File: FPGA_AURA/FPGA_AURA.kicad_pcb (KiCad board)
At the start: 10 copper layers, 50 x 50 mm, 191 parts, among them J1 ST5-40-1.00-L-D-P-TR, J100 USB_C_Receptacle_USB2.0_16P, J101 XT30PW-M, U1 XC7A35T-2FTG256C, U2 W25Q256JVEIQ, U200 ADP5014, U3 FT2232HQ, U4 TPS51200DRCR, U5 USBLC6-2SC6, U500 MT41K128M16JT-125_IT_K, U6 93LC56BT-I_SN, Y1 12MHz

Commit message: Continued DDR3 routing on top
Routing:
- net DDR3_A8: track 58.5 -> 76.5 mm
- net DDR3_BA1: track 0.57 -> 16.1 mm
- net DDR3_A3: track 3.18 -> 17.1 mm
- net DDR3_A0: track 4.63 -> 17.9 mm
- net DDR3_BA2: track 0.57 -> 8.20 mm
- net DDR3_A10: track 0.57 -> 5.79 mm
- net DDR3_CAS: track 0.57 -> 4.15 mm
- net DDR3_DQ1: track 49.4 -> 46.8 mm
- net DDR3_A12: track 0.57 -> 2.93 mm
- net DDR3_DQS0-: track 47.4 -> 46.5 mm
- net DDR3_ODT: track 1.27 -> 0.57 mm
- net DDR3_DQ2: track 47.3 -> 46.7 mm

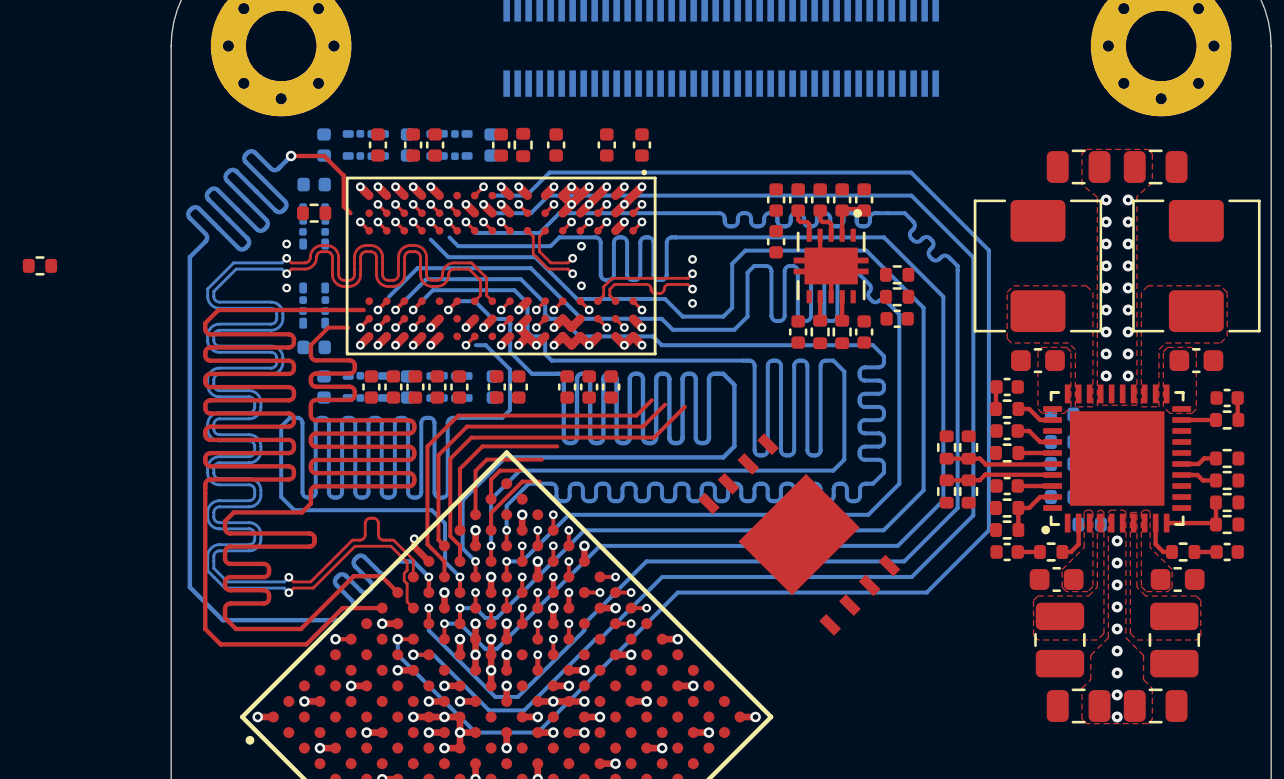
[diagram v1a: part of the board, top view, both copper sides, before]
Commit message: Continued DDR3 routing.
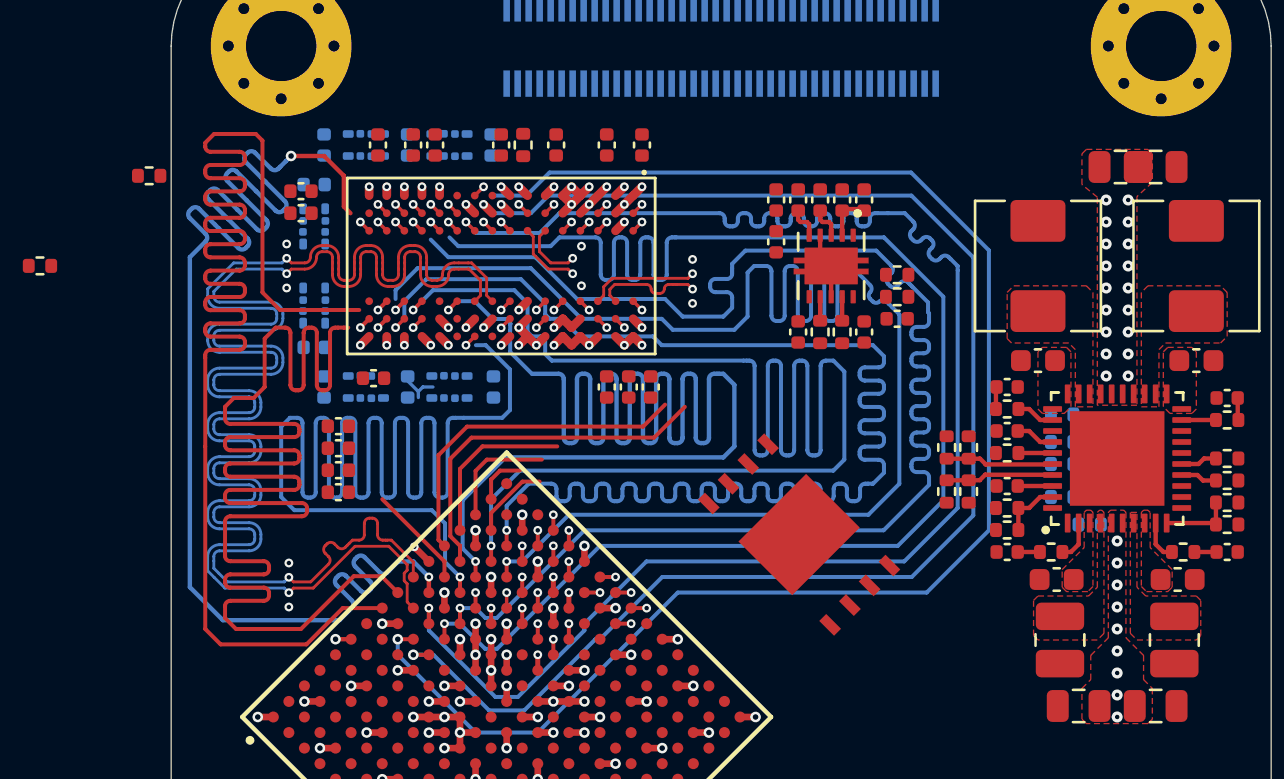
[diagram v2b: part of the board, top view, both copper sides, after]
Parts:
- moved C517 9.46 mm to (105.9, 61.6), turned to 180 degrees
- moved C512 8.95 mm to (105.9, 62.6), turned to 180 degrees
- moved C513 8.64 mm to (107.6, 75.3), turned to 180 degrees
- moved R524 7.69 mm to (99.0, 60.9)
- moved C511 6.68 mm to (107.6, 74.3), turned to 0 degrees
- moved C516 6.61 mm to (109.2, 70.1), turned to 180 degrees
- moved C510 5.29 mm to (107.6, 73.3), turned to 180 degrees
- moved C522 3.93 mm to (107.6, 72.3), turned to 180 degrees
- moved C206 1.90 mm to (143.2, 60.5)
- moved C514 1.80 mm to (121.8, 70.5)
- moved C519 1.80 mm to (120.8, 70.5)
- moved C523 1.80 mm to (119.8, 70.5)
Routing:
- net DDR3_A0: track 17.9 -> 5.27 mm
- net DDR3_A13: track 60.6 -> 70.4 mm
- net DDR3_A11: track 76.6 -> 71.4 mm
- net DDR3_A8: track 76.5 -> 71.4 mm
- net DDR3_RAS: track 70.1 -> 71.1 mm
- net GND: track 51.5 -> 52.4 mm, vias 87 -> 89
- net DDR3_CK-: track 71.6 -> 72.5 mm

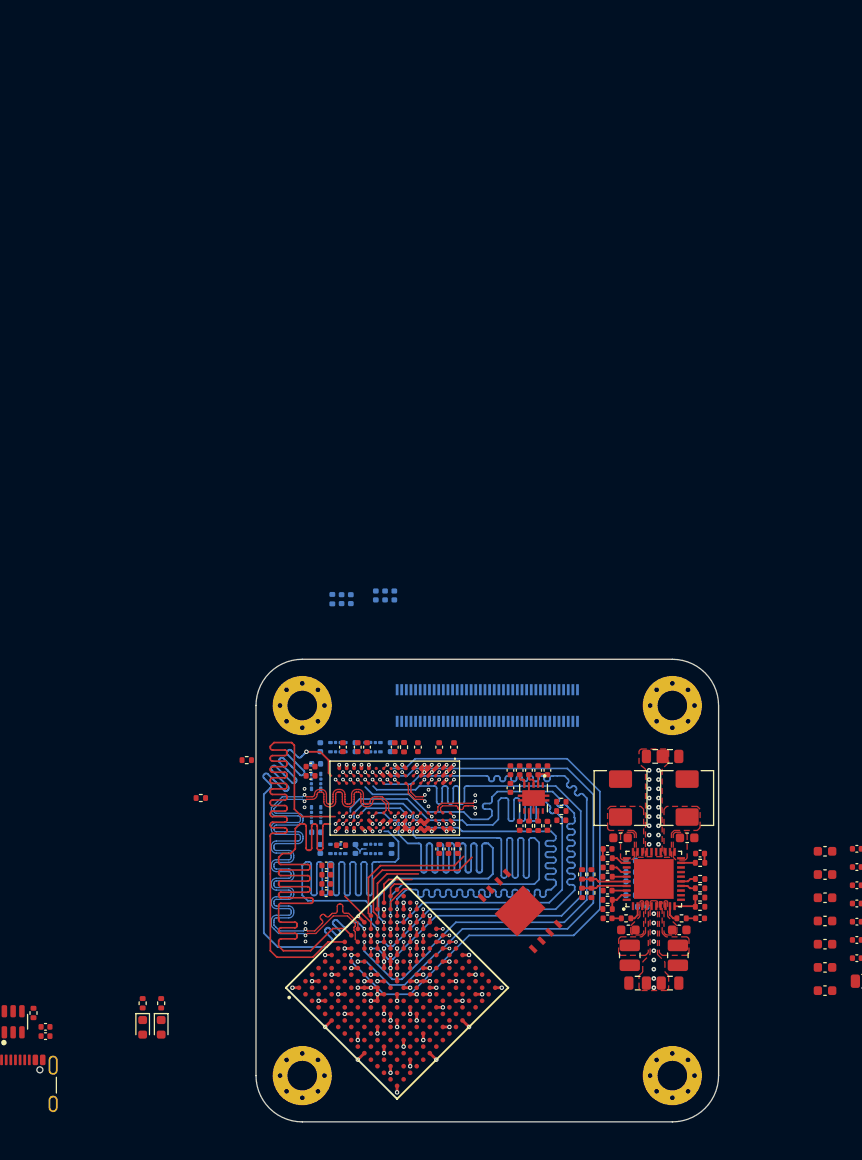
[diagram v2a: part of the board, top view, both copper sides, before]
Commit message: All DDR3 traces broken out, next stage is delay matching, and verifying break out through Vivado
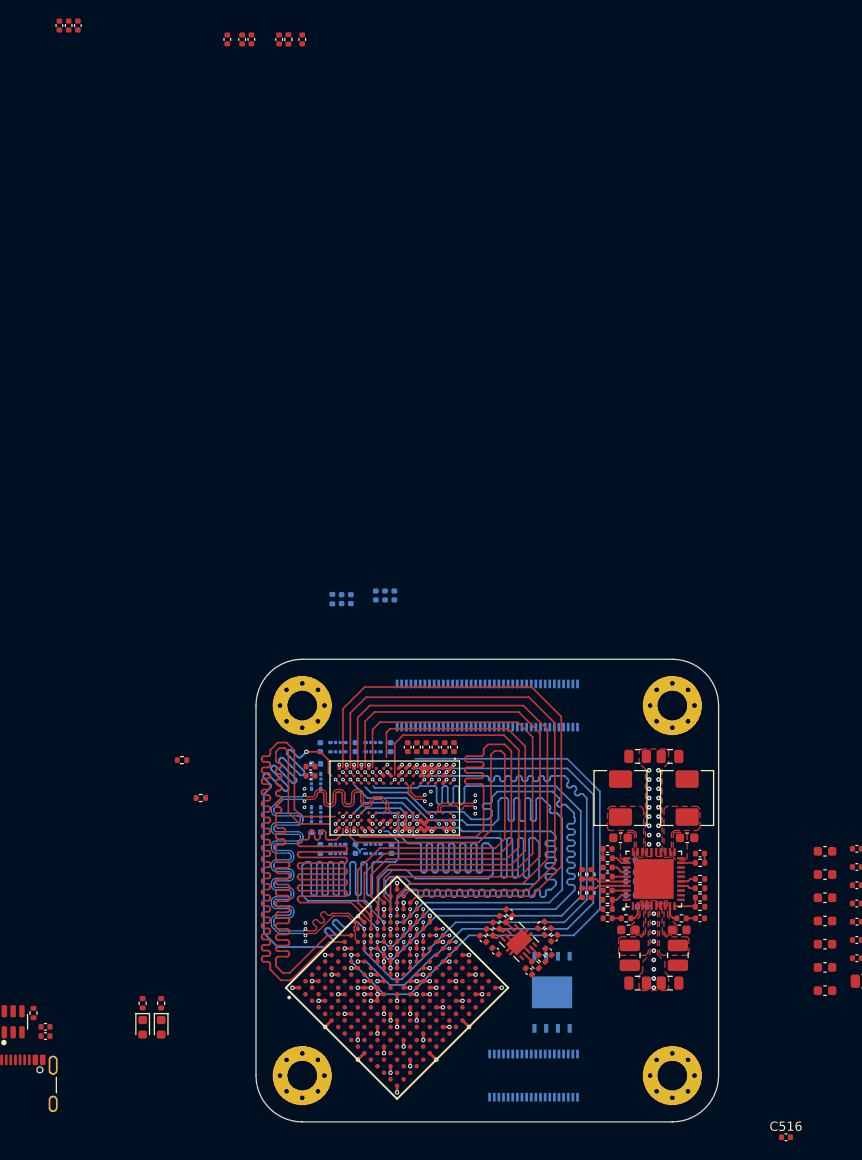
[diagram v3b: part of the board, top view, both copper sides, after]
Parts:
- added J2: SS5-20-3.00-X-D-K-XX, SS5-20-3.00-X-D-K-XX:SAMTEC_SS5-20-3.00-X-D-K-XX, B.Cu at (130.0, 95.0)
- J1: value ST5-40-1.00-L-D-P-TR -> SS5-40-3.00-X-D-K-XX; footprint ST5-40-1.00-L-D-P-TR:ST5-40-1.00-L-D-P-TR -> SS5-40-3.00-X-D-K-XX:SAMTEC_SS5-40-3.00-X-D-K-XX
- U2: moved to B.Cu
- moved C514 98.0 mm to (80.8, -18.5)
- moved C519 98.0 mm to (79.8, -18.5)
- moved C523 98.0 mm to (78.8, -18.5)
- moved C525 77.5 mm to (102.5, -17.0)
- moved C526 77.5 mm to (96.9, -17.0)
- moved C527 77.5 mm to (98.5, -17.0)
- moved C528 77.5 mm to (105.0, -17.0)
- moved C530 77.5 mm to (99.5, -17.0)
- moved R525 77.5 mm to (103.5, -17.0)
- moved C516 57.5 mm to (157.3, 101.7), turned to 0 degrees
- moved C513 19.7 mm to (119.4, 59.5), turned to 90 degrees
- moved C222 18.4 mm to (124.5, 80.2), turned to 135 degrees
- moved C219 17.8 mm to (125.3, 79.5), turned to 135 degrees
- moved C511 17.7 mm to (117.4, 59.5), turned to -90 degrees
- moved C508 17.7 mm to (125.9, 81.5), turned to -45 degrees
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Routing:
- net DDR3_A0: track 5.27 -> 76.6 mm
- net DDR3_ODT: track 0.57 -> 67.0 mm
- net DDR3_A1: track 0.57 -> 63.4 mm
- net DDR3_CS: track 0.57 -> 60.7 mm
- net DDR3_A12: track 2.93 -> 58.1 mm
- net DDR3_A3: track 17.1 -> 71.0 mm
- net DDR3_CAS: track 4.15 -> 56.3 mm
- net DDR3_A10: track 5.79 -> 50.7 mm
- net DDR3_BA1: track 16.1 -> 59.4 mm
- net DDR3_BA2: track 8.20 -> 50.1 mm
- net DDR3_A8: track 71.4 -> 76.2 mm
- net DDR3_A11: track 71.4 -> 76.1 mm
- net DDR3_A6: track 71.6 -> 67.4 mm
- net DDR3_A7: track 71.3 -> 68.3 mm
- net DDR3_A5: track 66.6 -> 63.6 mm
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
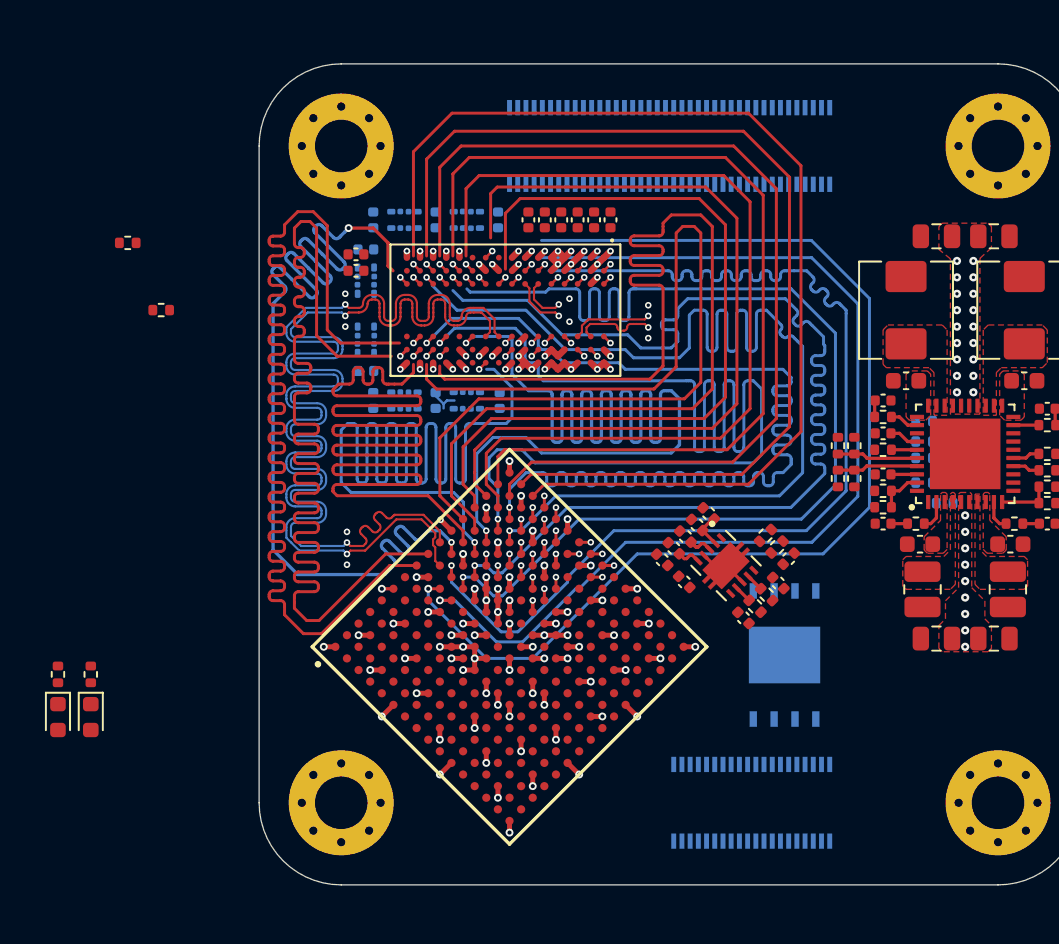
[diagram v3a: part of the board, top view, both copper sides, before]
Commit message: DDR3 Routing closed!
Finally DDR3 has been routed, verified, and length matched. Further validation still required.
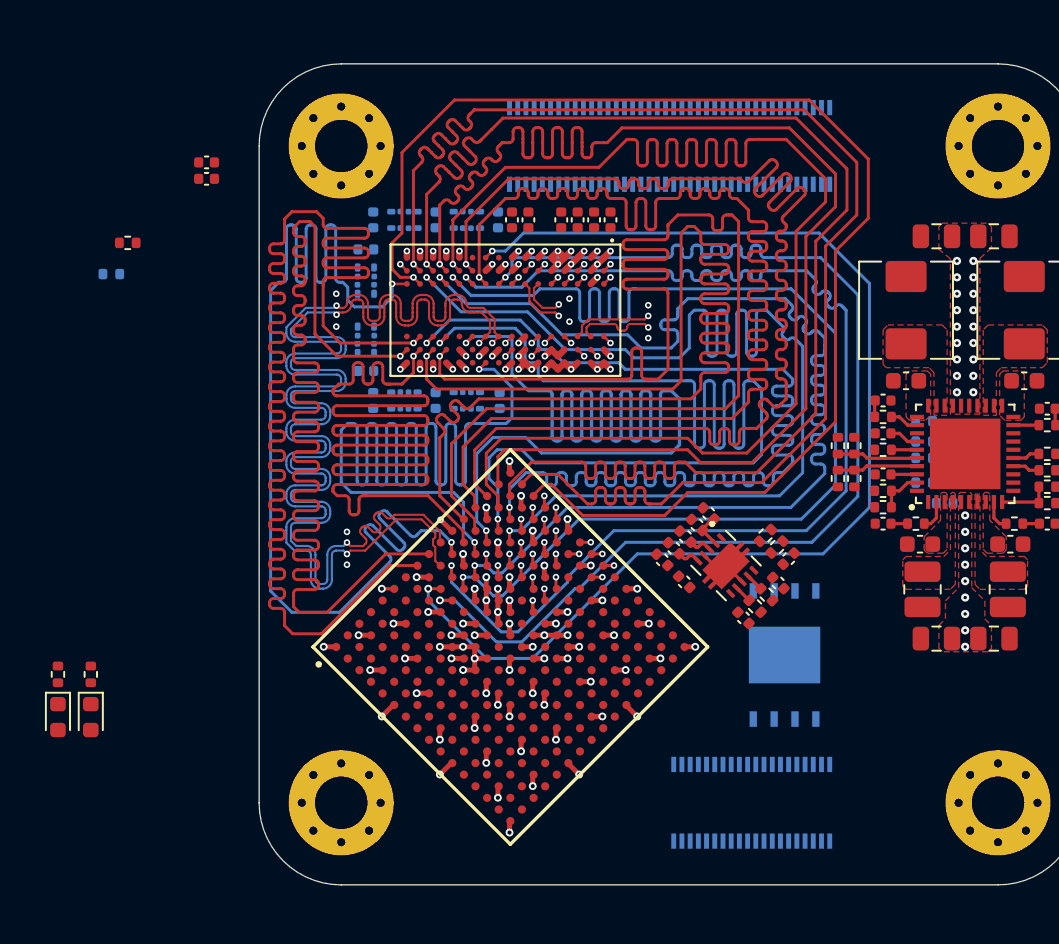
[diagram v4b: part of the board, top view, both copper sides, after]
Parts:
- R522: moved to B.Cu
- moved C512 10.7 mm to (96.8, 57.0)
- moved C517 10.7 mm to (96.8, 56.0)
- moved R522 3.75 mm to (91.0, 62.8), turned to 180 degrees
- moved C511 2.00 mm to (115.4, 59.5)
- moved U1 0.05 mm to (115.3, 85.5)
- turned C206 to 0 degrees
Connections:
- U1 pad A12: DDR3_BA1 -> DDR3_A4
- U1 pad A13: DDR3_BA2 -> DDR3_CAS
- U1 pad A14: DDR3_A10 -> DDR3_CS
- U1 pad A15: DDR3_A12 -> DDR3_A3
- U1 pad B10: DDR3_A4 -> DDR3_A13
- U1 pad B11: DDR3_A0 -> DDR3_A6
- U1 pad B12: DDR3_A3 -> DDR3_BA1
- U1 pad B14: DDR3_CAS -> DDR3_BA0
- U1 pad B15: DDR3_CS -> DDR3_A5
- U1 pad B16: DDR3_A1 -> DDR3_A7
- U1 pad C12: DDR3_BA0 -> DDR3_A10
- U1 pad C13: DDR3_A2 -> DDR3_A12
- U1 pad C14: DDR3_RAS -> DDR3_A1
- U1 pad C16: DDR3_ODT -> DDR3_A9
- U1 pad C8: DDR3_A7 -> DDR3_ODT
- U1 pad C9: DDR3_A6 -> DDR3_WE
- U1 pad D10: DDR3_A13 -> DDR3_A0
- U1 pad D13: DDR3_WE -> DDR3_A2
- U1 pad D8: DDR3_A5 -> DDR3_RAS
- U1 pad D9: DDR3_A9 -> DDR3_BA2
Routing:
- net DDR3_CAS: track 56.3 -> 84.0 mm
- net DDR3_BA1: track 59.4 -> 84.6 mm
- net DDR3_CS: track 60.7 -> 84.1 mm
- net DDR3_BA2: track 50.1 -> 72.2 mm, vias 1 -> 2
- net DDR3_A10: track 50.7 -> 72.3 mm, vias 1 -> 2
- net DDR3_A5: track 63.6 -> 84.4 mm, vias 2 -> 1
- net DDR3_A4: track 64.4 -> 84.4 mm, vias 3 -> 1
- net DDR3_A6: track 67.4 -> 84.4 mm, vias 2 -> 1
- net DDR3_A7: track 68.3 -> 84.5 mm, vias 2 -> 1
- net DDR3_A11: track 76.1 -> 91.7 mm
- net DDR3_A12: track 58.1 -> 72.4 mm, vias 1 -> 2
- net DDR3_A3: track 71.0 -> 84.4 mm
- net DDR3_BA0: track 72.9 -> 84.5 mm, vias 2 -> 1
- net DDR3_A9: track 70.5 -> 79.3 mm, vias 2 -> 1
- net DDR3_CK+: track 72.6 -> 81.1 mm, vias 2 -> 3
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
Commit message: Started pinout after successful Vivado bitstream generation.
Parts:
- removed C10, C102, C103, C12, C14, C17, C3, C4, C5, C6, C7, C8, C9: 100n, Capacitor_SMD:C_0402_1005Metric
- removed C100, C101: 47u, Capacitor_SMD:C_0805_2012Metric
- removed C104, C105: 1u, Capacitor_SMD:C_0402_1005Metric
- removed C11, C13, C2: 4u7, Capacitor_SMD:C_0402_1005Metric
- removed C15, C16: 27pF, Capacitor_SMD:C_0402_1005Metric
- removed D105, D106: LED, LED_SMD:LED_0603_1608Metric
- removed FB1, FB2: 120R, Inductor_SMD:L_0603_1608Metric
- removed J100: USB_C_Receptacle_USB2.0_16P, Connector_USB:USB_C_Receptacle_GCT_USB4105-xx-A_16P_TopMnt_Horizontal
- removed J101: XT30PW-M, XT30PWM:XT30PWM
- removed R100, R101: 5k1, Resistor_SMD:R_0402_1005Metric
- removed R108, R109, R4: 1k, Resistor_SMD:R_0402_1005Metric
- removed R2, R3: 22R, Resistor_SMD:R_0402_1005Metric
- removed R5, R6: 12k, Resistor_SMD:R_0402_1005Metric
- removed U3: FT2232HQ, FT2232HQ:QFN50P900X900X100-65N
- removed U5: USBLC6-2SC6, Package_TO_SOT_SMD:SOT-23-6
- removed U6: 93LC56BT-I_SN, 93LC56BT-I_SN:SOIC127P600X175-8N
- removed Y1: 12MHz, X322512MSB4SI:X322512MSB4SI
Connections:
- net 200MHz_CC_P renamed 100MHz_CC
- U1 pad A5: unconnected-(U1F-IO_L3P_T0_DQS_AD5P_35-PadA5) -> PHY_1_RST
- U1 pad A7: unconnected-(U1F-IO_L1N_T0_AD4N_35-PadA7) -> MDIO
- U1 pad B5: unconnected-(U1F-IO_L2N_T0_AD12N_35-PadB5) -> PHY_0_RST
- U1 pad B7: unconnected-(U1F-IO_L1P_T0_AD4P_35-PadB7) -> MDC
- U1 pad E1: unconnected-(U1F-IO_L15N_T2_DQS_35-PadE1) -> ETH_1_RX_2
- U1 pad E5: unconnected-(U1F-IO_L13N_T2_MRCC_35-PadE5) -> ETH_1_RXC
- U1 pad F2: unconnected-(U1F-IO_L15P_T2_DQS_35-PadF2) -> ETH_1_RX_1
- U1 pad F3: unconnected-(U1F-IO_L14N_T2_SRCC_35-PadF3) -> ETH_1_RX_0
- U1 pad F5: unconnected-(U1F-IO_L13P_T2_MRCC_35-PadF5) -> ETH_0_RXC
- U1 pad G1: unconnected-(U1F-IO_L17N_T2_35-PadG1) -> ETH_1_TD_1
- U1 pad G2: unconnected-(U1F-IO_L17P_T2_35-PadG2) -> ETH_1_TD_0
- U1 pad G4: unconnected-(U1F-IO_L16N_T2_35-PadG4) -> ETH_1_RX_CTL
- U1 pad G5: unconnected-(U1F-IO_L16P_T2_35-PadG5) -> ETH_1_RX_3
- U1 pad H1: unconnected-(U1F-IO_L20N_T3_35-PadH1) -> ETH_0_RX_1
- U1 pad H2: unconnected-(U1F-IO_L20P_T3_35-PadH2) -> ETH_0_RX_0
- U1 pad H3: unconnected-(U1F-IO_L21N_T3_DQS_35-PadH3) -> ETH_0_RX_3
- U1 pad H4: unconnected-(U1F-IO_L18N_T2_35-PadH4) -> ETH_1_TD_3
- U1 pad H5: unconnected-(U1F-IO_L18P_T2_35-PadH5) -> ETH_1_TD_2
- U1 pad J1: unconnected-(U1F-IO_L22N_T3_35-PadJ1) -> ETH_0_TD_0
- U1 pad J3: unconnected-(U1F-IO_L21P_T3_DQS_35-PadJ3) -> ETH_0_RX_2
- U1 pad J4: unconnected-(U1F-IO_L19N_T3_VREF_35-PadJ4) -> ETH_1_TXC
- U1 pad J5: unconnected-(U1F-IO_L19P_T3_35-PadJ5) -> ETH_1_TX_CTL
- U1 pad K1: unconnected-(U1F-IO_L22P_T3_35-PadK1) -> ETH_0_RX_CTL
- U1 pad K12: unconnected-(U1C-IO_0_14-PadK12) -> SYS_nRST
- U1 pad K2: unconnected-(U1F-IO_L24N_T3_35-PadK2) -> ETH_0_TX_CTL
- U1 pad K3: unconnected-(U1F-IO_L24P_T3_35-PadK3) -> ETH_0_TD_3
- U1 pad K5: unconnected-(U1F-IO_25_35-PadK5) -> ETH_0_TXC
- U1 pad L13: INIT_CALIB_DONE -> unconnected-(U1C-IO_L5N_T0_D07_14-PadL13)
- U1 pad L14: TG_COMP_ERR -> unconnected-(U1C-IO_L4P_T0_D04_14-PadL14)
- U1 pad L2: unconnected-(U1F-IO_L23N_T3_35-PadL2) -> ETH_0_TD_2
- U1 pad L3: unconnected-(U1F-IO_L23P_T3_35-PadL3) -> ETH_0_TD_1
- U1 pad L7: Net-(U1A-TCK_0) -> unconnected-(U1A-TCK_0-PadL7)
- U1 pad M14: SYS_RST -> INIT_CALIB_DONE
- U1 pad M6: unconnected-(U1C-IO_L19P_T3_A10_D26_14-PadM6) -> SPI_CS
- U1 pad M7: Net-(U1A-TMS_0) -> unconnected-(U1A-TMS_0-PadM7)
- U1 pad N12: 200MHz_CC_N -> unconnected-(U1C-IO_L13N_T2_MRCC_14-PadN12)
- U1 pad N6: unconnected-(U1C-IO_L19N_T3_A09_D25_VREF_14-PadN6) -> SPI_SCK
- U1 pad N7: Net-(U1A-TDI_0) -> unconnected-(U1A-TDI_0-PadN7)
- U1 pad N8: Net-(U1A-TDO_0) -> unconnected-(U1A-TDO_0-PadN8)
- U1 pad P8: unconnected-(U1C-IO_L20P_T3_A08_D24_14-PadP8) -> SPI_MOSI
- U1 pad R6: unconnected-(U1C-IO_L24P_T3_A01_D17_14-PadR6) -> UART_TX
- U1 pad R7: unconnected-(U1C-IO_L24N_T3_A00_D16_14-PadR7) -> UART_RX
- U1 pad R8: unconnected-(U1C-IO_L20N_T3_A07_D23_14-PadR8) -> SPI_MISO
